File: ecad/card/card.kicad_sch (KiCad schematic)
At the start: 138 parts, among them J1 Conn_01x03_Pin, J2 USB4105-GF-A, J3 10145226-0241N13LF, J4 Conn_01x03_Pin, SW1 SW_Push, SW2 SW_Push, U1 W25Q128JVS, U2 RP2350_80QFN, U3 MCP23017_SO, U4 NCP1117-3.3_SOT223, U5 MCP23017_SO, X1 ABM8-272-T3

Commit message: Back panel changes
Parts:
- removed D2: D_Schottky, Diode_SMD:D_0402_1005Metric, symbol Device:D_Schottky
- added D4: D_Schottky, Diode_SMD:D_0402_1005Metric, symbol Device:D_Schottky
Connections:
- net 3.3V: now also D4.1 (K); no longer C23.1, U4.2 (VO)
- new net: C23.1, D4.2 (A), U4.2 (VO)
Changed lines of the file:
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@@
 	)
 	(junction
-		(at 204.47 132.08)
-		(diameter 0)
-		(color 0 0 0 0)
-	)
-	(junction
 		(at 30.48 74.93)
 		(diameter 0)
@@
 	)
 	(junction
+		(at 204.47 132.08)
+		(diameter 0)
+		(color 0 0 0 0)
+	)
+	(junction
 		(at 154.94 27.94)
 		(diameter 0)
@@
 	(polyline
 		(pts
-			(xy 216.154 136.398) (xy 216.154 147.066)
+			(xy 215.9 130.048) (xy 215.9 147.066)
 		)
 		(stroke
@@
 	(wire
 		(pts
-			(xy 204.47 119.38) (xy 204.47 132.08)
-		)
-		(stroke
-			(width 0)
-			(type default)
-		)
-	)
-	(wire
-		(pts
 			(xy 222.25 58.42) (xy 219.71 58.42)
 		)
@@
 	(polyline
 		(pts
-			(xy 216.154 111.76) (xy 216.154 136.398)
+			(xy 215.9 105.41) (xy 215.9 130.048)
 		)
 		(stroke
@@
 	(wire
 		(pts
+			(xy 204.47 115.57) (xy 204.47 119.38)
+		)
+		(stroke
+			(width 0)
+			(type default)
+		)
+	)
+	(wire
+		(pts
 			(xy 104.14 199.39) (xy 104.14 201.93)
 		)
@@
 	(polyline
 		(pts
-			(xy 166.37 147.066) (xy 166.37 111.76)
+			(xy 166.116 147.066) (xy 166.116 105.41)
 		)
 		(stroke
@@
 	(wire
 		(pts
-			(xy 173.99 119.38) (xy 173.99 132.08)
+			(xy 233.68 78.74) (xy 233.68 81.28)
 		)
 		(stroke
@@
 	(wire
 		(pts
-			(xy 233.68 78.74) (xy 233.68 81.28)
+			(xy 265.43 212.09) (xy 273.05 212.09)
 		)
 		(stroke
@@
 	(wire
 		(pts
-			(xy 265.43 212.09) (xy 273.05 212.09)
+			(xy 118.11 50.8) (xy 118.11 52.07)
 		)
 		(stroke
@@
 	(wire
 		(pts
-			(xy 118.11 50.8) (xy 118.11 52.07)
+			(xy 204.47 127) (xy 204.47 132.08)
 		)
 		(stroke
@@
 	(polyline
 		(pts
-			(xy 166.37 111.76) (xy 216.154 111.76)
+			(xy 166.116 105.41) (xy 215.9 105.41)
 		)
 		(stroke
@@
 	(global_label "3.3V"
 		(shape input)
-		(at 204.47 119.38 90)
+		(at 204.47 115.57 90)
 		(fields_autoplaced yes)
 		(effects
@@
 		)
 		(property "Intersheetrefs" "${INTERSHEET_REFS}"
-			(at 204.47 112.2824 90)
+			(at 204.47 108.4724 90)
 			(effects
 				(font
@@
 	)
 	(symbol
-		(lib_id "Device:D_Schottky")
-		(at 204.47 114.3 270)
-		(unit 1)
-		(exclude_from_sim no)
-		(in_bom yes)
-		(on_board yes)
-		(dnp no)
-		(fields_autoplaced yes)
-		(property "Reference" "D2"
-			(at 207.01 112.7124 90)
-			(effects
-				(font
-					(size 1.27 1.27)
-				)
-				(justify left)
-			)
-		)
-		(property "Value" "D_Schottky"
-			(at 207.01 115.2524 90)
-			(effects
-				(font
-					(size 1.27 1.27)
-				)
-				(justify left)
-			)
-		)
-		(property "Footprint" "Diode_SMD:D_0402_1005Metric"
-			(at 204.47 114.3 0)
-			(effects
-				(font
-					(size 1.27 1.27)
-				)
-				(hide yes)
-			)
-		)
-		(property "Datasheet" "~"
-			(at 204.47 114.3 0)
-			(effects
-				(font
-					(size 1.27 1.27)
-				)
-				(hide yes)
-			)
-		)
-		(property "Description" "Schottky diode"
-			(at 204.47 114.3 0)
-			(effects
-				(font
-					(size 1.27 1.27)
-				)
-				(hide yes)
-			)
-		)
-		(pin "1"
-		)
-		(pin "2"
-		)
-		(instances
-			(project "card"
-				(path "/9dd060f0-80a5-46f7-bd5a-b7a0ead0972f"
-					(reference "D2")
-					(unit 1)
-				)
-			)
-		)
-	)
-	(symbol
 		(lib_id "Device:R_Small")
 		(at 275.59 212.09 90)
@@
 					(unit 1)
 				)
+			)
+		)
+	)
+	(symbol
+		(lib_id "Device:D_Schottky")
+		(at 204.47 123.19 270)
+		(unit 1)
+		(exclude_from_sim no)
+		(in_bom yes)
+		(on_board yes)
+		(dnp no)
+		(fields_autoplaced yes)
+		(property "Reference" "D4"
+			(at 207.01 121.6024 90)
+			(effects
+				(font
+					(size 1.27 1.27)
+				)
+				(justify left)
+			)
+		)
+		(property "Value" "D_Schottky"
+			(at 207.01 124.1424 90)
+			(effects
+				(font
+					(size 1.27 1.27)
+				)
+				(justify left)
+			)
+		)
+		(property "Footprint" "Diode_SMD:D_0402_1005Metric"
+			(at 204.47 123.19 0)
+			(effects
+				(font
+					(size 1.27 1.27)
+				)
+				(hide yes)
+			)
+		)
+		(property "Datasheet" "~"
+			(at 204.47 123.19 0)
+			(effects
+				(font
+					(size 1.27 1.27)
+				)
+				(hide yes)
+			)
+		)
+		(property "Description" "Schottky diode"
+			(at 204.47 123.19 0)
+			(effects
+				(font
+					(size 1.27 1.27)
+				)
+				(hide yes)
+			)
+		)
+		(pin "1"
+		)
+		(pin "2"
+		)
+		(instances
+			(project "card"
+				(path "/9dd060f0-80a5-46f7-bd5a-b7a0ead0972f"
+					(reference "D4")
+					(unit 1)
+				)

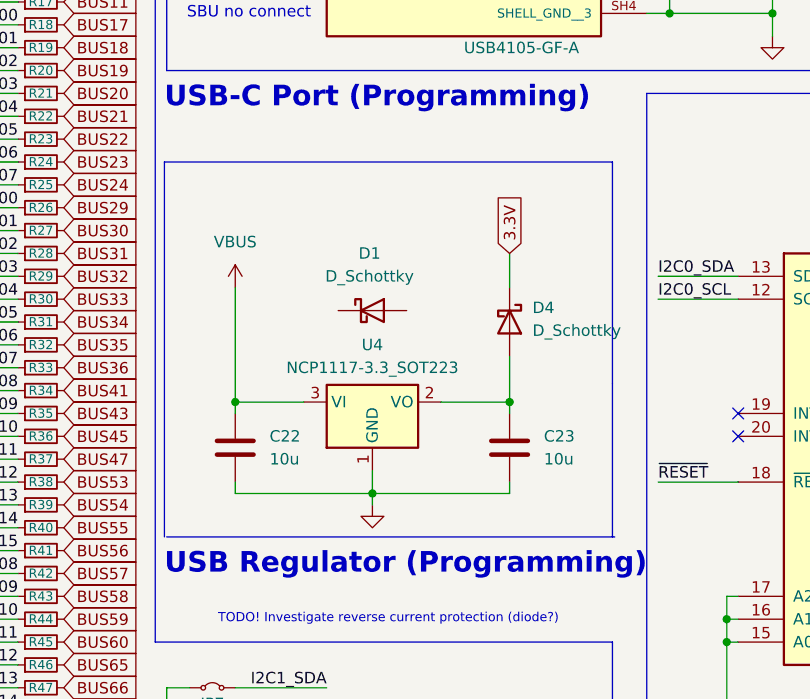
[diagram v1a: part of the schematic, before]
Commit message: new diode, some panel pwr routing
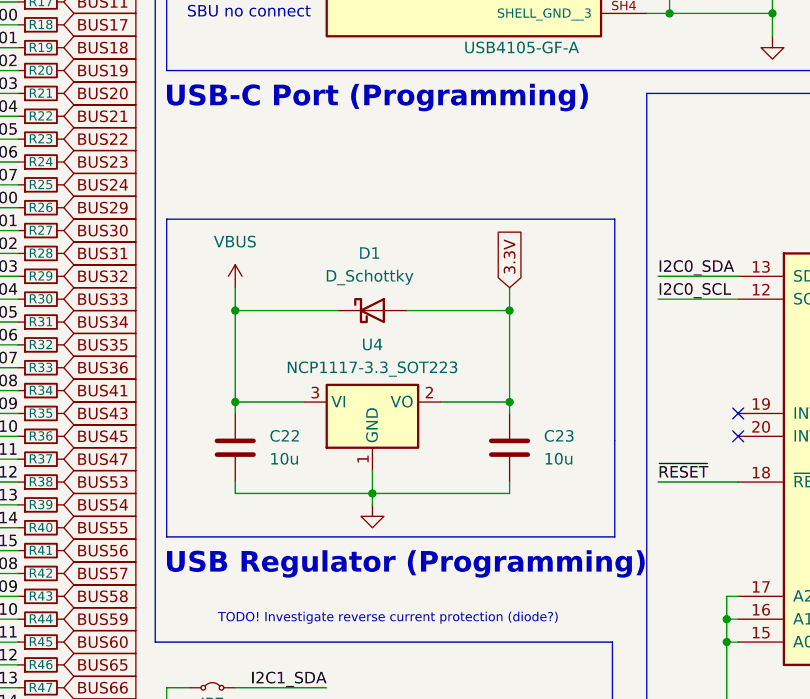
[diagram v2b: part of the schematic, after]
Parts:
- removed D4: D_Schottky, Diode_SMD:D_0402_1005Metric, symbol Device:D_Schottky
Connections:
- net 3.3V: now also C23.1, D1.2 (A), U4.2 (VO)
- net VBUS: now also D1.1 (K)
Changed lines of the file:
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@@
 	)
 	(junction
+		(at 204.47 121.92)
+		(diameter 0)
+		(color 0 0 0 0)
+	)
+	(junction
 		(at 166.37 194.31)
 		(diameter 0)
@@
 	)
 	(junction
+		(at 173.99 121.92)
+		(diameter 0)
+		(color 0 0 0 0)
+	)
+	(junction
 		(at 222.25 78.74)
 		(diameter 0)
@@
 	)
 	(junction
+		(at 204.47 132.08)
+		(diameter 0)
+		(color 0 0 0 0)
+	)
+	(junction
 		(at 30.48 74.93)
 		(diameter 0)
@@
 	)
 	(junction
-		(at 204.47 132.08)
-		(diameter 0)
-		(color 0 0 0 0)
-	)
-	(junction
 		(at 154.94 27.94)
 		(diameter 0)
@@
 	(polyline
 		(pts
-			(xy 215.9 130.048) (xy 215.9 147.066)
+			(xy 216.154 136.398) (xy 216.154 147.066)
 		)
 		(stroke
@@
 	(wire
 		(pts
+			(xy 204.47 119.38) (xy 204.47 121.92)
+		)
+		(stroke
+			(width 0)
+			(type default)
+		)
+	)
+	(wire
+		(pts
 			(xy 222.25 58.42) (xy 219.71 58.42)
 		)
@@
 	(wire
 		(pts
+			(xy 193.04 121.92) (xy 204.47 121.92)
+		)
+		(stroke
+			(width 0)
+			(type default)
+		)
+	)
+	(wire
+		(pts
 			(xy 143.51 36.83) (xy 143.51 38.1)
 		)
@@
 	(polyline
 		(pts
-			(xy 215.9 105.41) (xy 215.9 130.048)
+			(xy 216.154 111.76) (xy 216.154 136.398)
 		)
 		(stroke
@@
 	(wire
 		(pts
-			(xy 204.47 115.57) (xy 204.47 119.38)
-		)
-		(stroke
-			(width 0)
-			(type default)
-		)
-	)
-	(wire
-		(pts
 			(xy 104.14 199.39) (xy 104.14 201.93)
 		)
@@
 	(polyline
 		(pts
-			(xy 166.116 147.066) (xy 166.116 105.41)
+			(xy 166.37 147.066) (xy 166.37 111.76)
 		)
 		(stroke
@@
 	(wire
 		(pts
+			(xy 173.99 121.92) (xy 185.42 121.92)
+		)
+		(stroke
+			(width 0)
+			(type default)
+		)
+	)
+	(wire
+		(pts
 			(xy 97.79 27.94) (xy 97.79 29.21)
 		)
@@
 	(wire
 		(pts
-			(xy 140.97 143.51) (xy 149.86 143.51)
+			(xy 204.47 121.92) (xy 204.47 132.08)
 		)
 		(stroke
@@
 	(wire
 		(pts
-			(xy 67.31 194.31) (xy 72.39 194.31)
+			(xy 140.97 143.51) (xy 149.86 143.51)
 		)
 		(stroke
@@
 	(wire
 		(pts
-			(xy 265.43 222.25) (xy 273.05 222.25)
+			(xy 67.31 194.31) (xy 72.39 194.31)
 		)
 		(stroke
@@
 	(wire
 		(pts
-			(xy 219.71 55.88) (xy 222.25 55.88)
+			(xy 265.43 222.25) (xy 273.05 222.25)
 		)
 		(stroke
@@
 	(wire
 		(pts
-			(xy 173.99 119.38) (xy 173.99 132.08)
+			(xy 219.71 55.88) (xy 222.25 55.88)
 		)
 		(stroke
@@
 	(wire
 		(pts
-			(xy 233.68 78.74) (xy 233.68 81.28)
+			(xy 173.99 119.38) (xy 173.99 121.92)
 		)
 		(stroke
@@
 	(wire
 		(pts
-			(xy 265.43 212.09) (xy 273.05 212.09)
+			(xy 233.68 78.74) (xy 233.68 81.28)
 		)
 		(stroke
@@
 	(wire
 		(pts
-			(xy 118.11 50.8) (xy 118.11 52.07)
+			(xy 265.43 212.09) (xy 273.05 212.09)
 		)
 		(stroke
@@
 	(wire
 		(pts
-			(xy 204.47 127) (xy 204.47 132.08)
+			(xy 118.11 50.8) (xy 118.11 52.07)
 		)
 		(stroke
@@
 		)
 	)
+	(wire
+		(pts
+			(xy 173.99 121.92) (xy 173.99 132.08)
+		)
+		(stroke
+			(width 0)
+			(type default)
+		)
+	)
 	(polyline
 		(pts
@@
 	(polyline
 		(pts
-			(xy 166.116 105.41) (xy 215.9 105.41)
+			(xy 166.37 111.76) (xy 216.154 111.76)
 		)
 		(stroke
@@
 	(global_label "3.3V"
 		(shape input)
-		(at 204.47 115.57 90)
+		(at 204.47 119.38 90)
 		(fields_autoplaced yes)
 		(effects
@@
 		)
 		(property "Intersheetrefs" "${INTERSHEET_REFS}"
-			(at 204.47 108.4724 90)
+			(at 204.47 112.2824 90)
 			(effects
 				(font
@@
 					(unit 1)
 				)
-			)
-		)
-	)
-	(symbol
-		(lib_id "Device:D_Schottky")
-		(at 204.47 123.19 270)
-		(unit 1)
-		(exclude_from_sim no)
-		(in_bom yes)
-		(on_board yes)
-		(dnp no)
-		(fields_autoplaced yes)
-		(property "Reference" "D4"
-			(at 207.01 121.6024 90)
-			(effects
-				(font
-					(size 1.27 1.27)
-				)
-				(justify left)
-			)
-		)
-		(property "Value" "D_Schottky"
-			(at 207.01 124.1424 90)
-			(effects
-				(font
-					(size 1.27 1.27)
-				)
-				(justify left)
-			)
-		)
-		(property "Footprint" "Diode_SMD:D_0402_1005Metric"
-			(at 204.47 123.19 0)
-			(effects
-				(font
-					(size 1.27 1.27)
-				)
-				(hide yes)
-			)
-		)
-		(property "Datasheet" "~"
-			(at 204.47 123.19 0)
-			(effects
-				(font
-					(size 1.27 1.27)
-				)
-				(hide yes)
-			)
-		)
-		(property "Description" "Schottky diode"
-			(at 204.47 123.19 0)
-			(effects
-				(font
-					(size 1.27 1.27)
-				)
-				(hide yes)
-			)
-		)
-		(pin "1"
-		)
-		(pin "2"
-		)
-		(instances
-			(project "card"
-				(path "/9dd060f0-80a5-46f7-bd5a-b7a0ead0972f"
-					(reference "D4")
-					(unit 1)
-				)

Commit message: card connector, diode changes
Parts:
- removed D2: Debugging, Diode_SMD:D_0402_1005Metric_Pad0.77x0.64mm_HandSolder, symbol Device:D
- removed D3: Protection, Diode_SMD:D_0402_1005Metric_Pad0.77x0.64mm_HandSolder, symbol Device:D_Schottky
- added J5: Conn_01x03_Pin, Connector_JST:JST_XH_S3B-XH-A-1_1x03_P2.50mm_Horizontal, symbol Connector:Conn_01x03_Pin
- D1: footprint Diode_SMD:D_0402_1005Metric_Pad0.77x0.64mm_HandSolder -> Library:DO-214BA_MCH-M
- J1, J4: footprint Connector_JST:JST_XH_B3B-XH-AM_1x03_P2.50mm_Vertical -> Connector_JST:JST_XH_S3B-XH-A-1_1x03_P2.50mm_Horizontal
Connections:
- net GND: now also J5.2 (Pin_2)
- net I2C1_SCL: now also J5.3 (Pin_3)
- net I2C1_SDA: now also J5.1 (Pin_1)

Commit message: Card BOM
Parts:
- C1, C4: JLCPCB Part # (none) -> C1570
- C10, C11, C12, C13, C14, C15, C16, C17, C18, C19, C20, C24, C3, C6, C9: JLCPCB Part # (none) -> C1525
- C2, C5, C7, C8: JLCPCB Part # (none) -> C23733
- C21, C22, C23: JLCPCB Part # (none) -> C15525
- D1: JLCPCB Part # (none) -> C3757764
- L1: JLCPCB Part # (none) -> C42411119
- R1, R3, R4: JLCPCB Part # (none) -> C11702
- R10, R9: JLCPCB Part # (none) -> C25905
- R11, R12, R13, R14, R15, R16, R17, R18, R19, R20, R21, R22, R23, R24, R25, R26, R27, R28, R29, R30, R31, R32, R33, R34, R35, R36, R37, R38, R39, R40, R41, R42, R43, R44, R45, R46, R47, R48, R49, R50, R51, R52, R53, R54, R55, R56, R57, R58, R59, R60, R61, R62, R63, R64, R65, R66, R67, R68, R69, R70, R71, R72, R73, R74, R75, R76, R77, R78, R79, R8, R80, R81, R82, R83, R84, R85, R86, R87, R88, R89: JLCPCB Part # (none) -> C25104
- R2: JLCPCB Part # (none) -> C25105
- R5, R6: JLCPCB Part # (none) -> C138021
- R7: JLCPCB Part # (none) -> C25741
- U1: JLCPCB Part # (none) -> C97521
- U2: JLCPCB Part # (none) -> C42415655
- U3, U5: JLCPCB Part # (none) -> C639770
- U4: JLCPCB Part # (none) -> C26537
- X1: JLCPCB Part # (none) -> C20625731
